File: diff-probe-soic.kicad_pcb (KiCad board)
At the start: 4 copper layers, 75 x 25 mm, 34 parts, among them J1 Conn_01x02, J2 Conn_Coaxial, J3 Conn_01x03, U1 LTC6228xS8, U2 LTC6228xS8, U3 LTC6228xS8

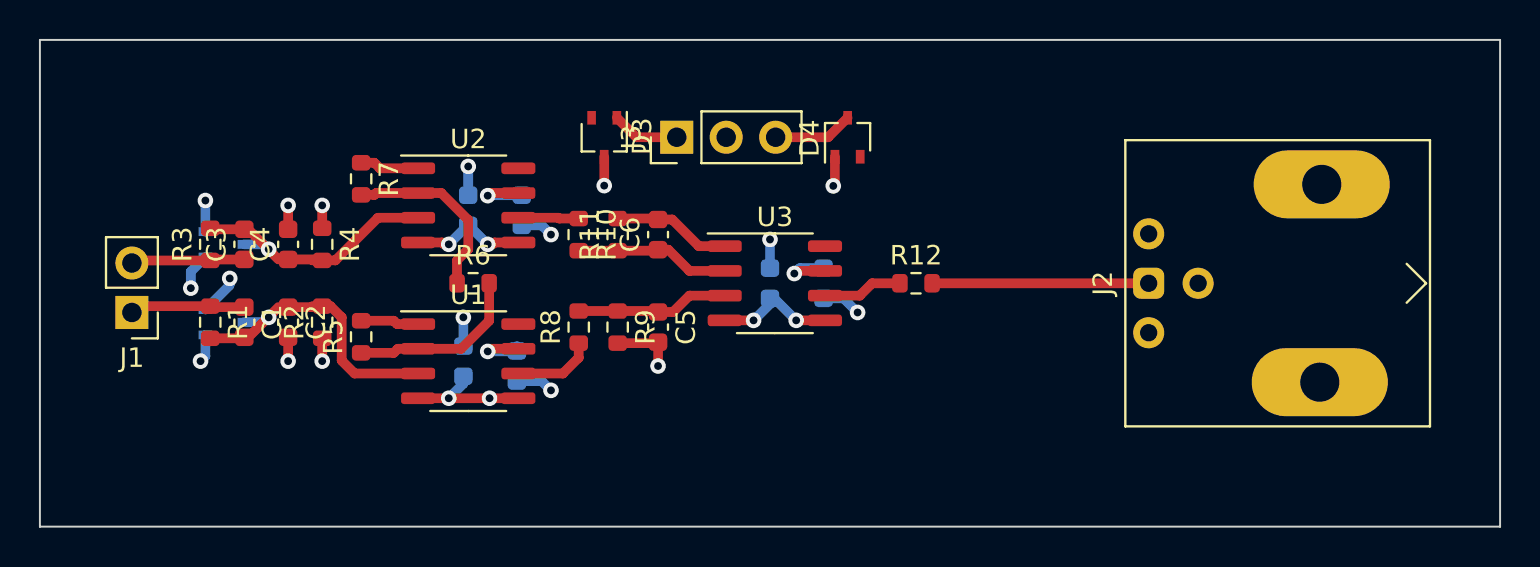
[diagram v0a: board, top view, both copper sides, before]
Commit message: Removed input diodes. Rerouted VDD and VSS.
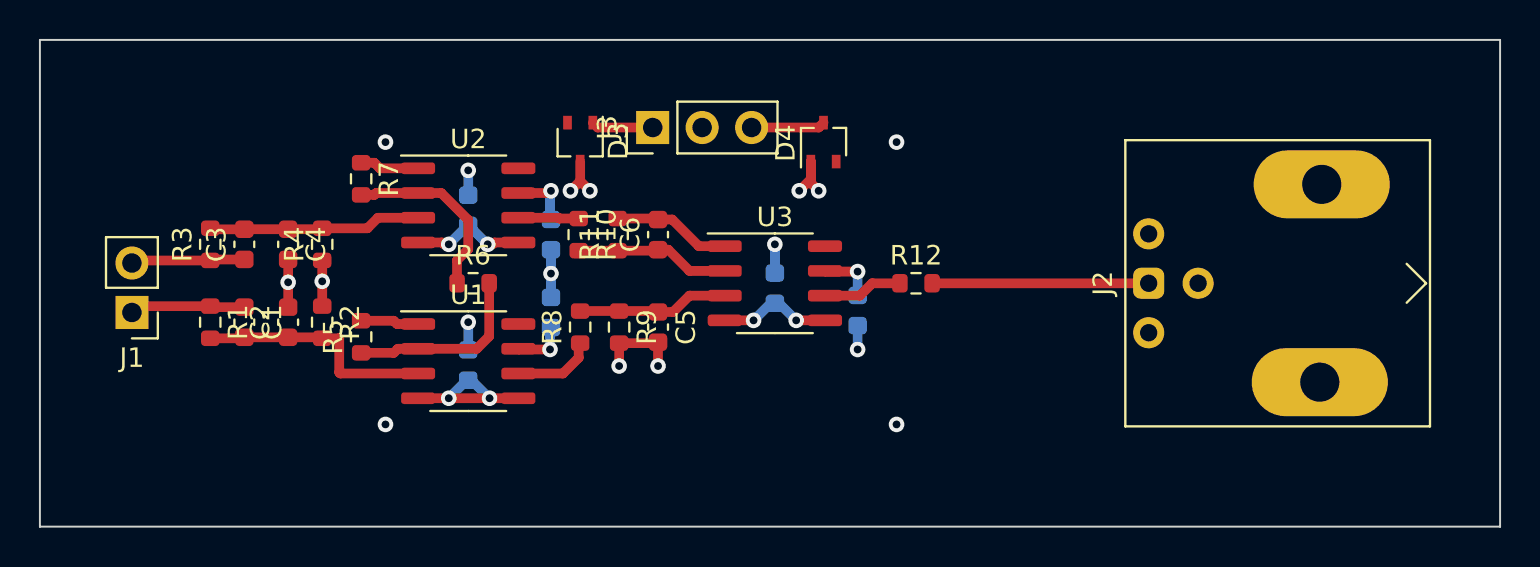
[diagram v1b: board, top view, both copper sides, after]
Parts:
- removed D1, D2: BAT54SW, Package_TO_SOT_SMD:SOT-323_SC-70
- moved C10 3.26 mm to (56.2, 51.5), turned to 90 degrees
- moved C30 2.24 mm to (72.0, 51.4)
- moved C20 1.95 mm to (56.2, 47.5)
- moved J3 1.33 mm to (61.5, 42.0)
- moved D3 1.26 mm to (57.8, 42.8)
- moved D4 1.26 mm to (70.2, 42.8)
- moved C31 0.35 mm to (67.8, 50.2)
- moved C11 0.32 mm to (52.0, 54.2)
- moved R8 0.08 mm to (57.8, 52.2)
- moved R9 0.08 mm to (59.8, 52.2)
- turned C2 to 90 degrees
- turned C4 to -90 degrees
- turned R2 to -90 degrees
- turned R4 to 90 degrees
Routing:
- net VDD: track 66.1 -> 11.2 mm, vias 6 -> 5
- net VSS: track 76.0 -> 23.1 mm, vias 9 -> 8
- net /ATTEN_POS: track 15.3 -> 12.5 mm, vias 1 -> 0
- net /ATTEN_NEG: track 13.5 -> 11.2 mm, vias 1 -> 0
- net GND: track 18.4 -> 16.4 mm, vias 11 -> 13

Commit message: cleaned up power planes. Power connector on south edge. BNC connector is wrong footprint.
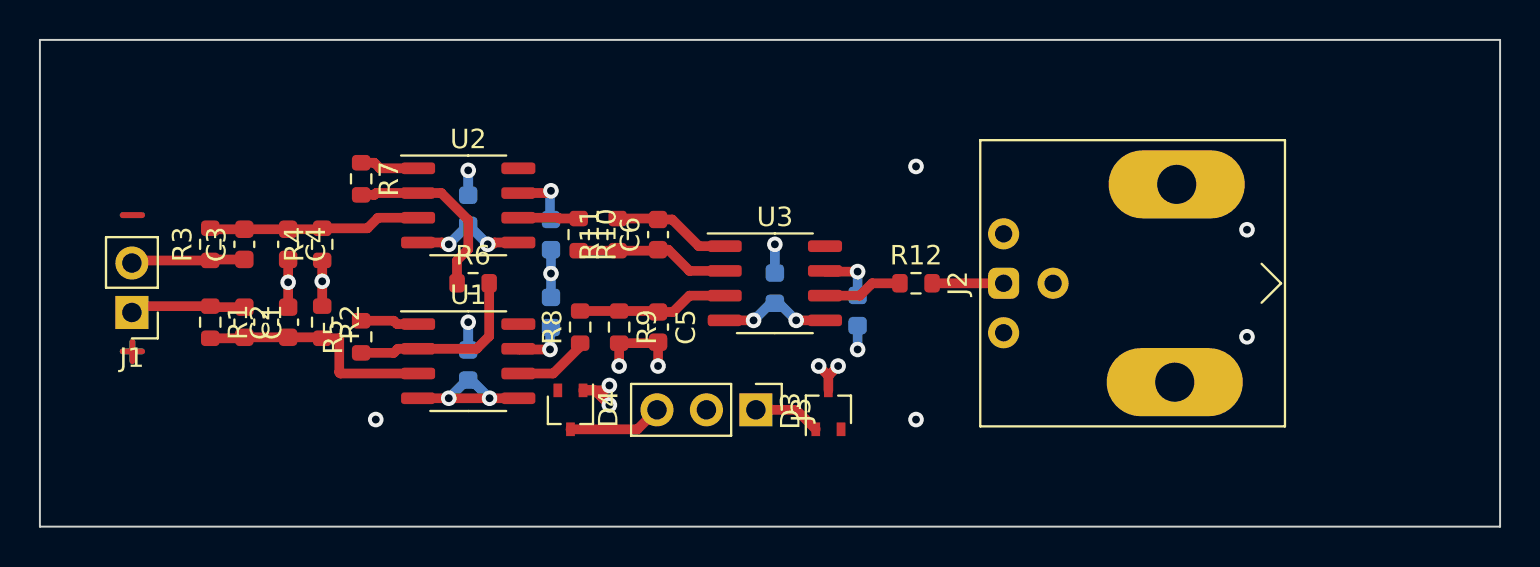
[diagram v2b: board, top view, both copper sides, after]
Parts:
- moved D4 18.9 mm to (57.2, 56.5), turned to -90 degrees
- moved D3 18.8 mm to (70.5, 56.5), turned to 90 degrees
- moved J3 15.4 mm to (66.8, 56.5), turned to -90 degrees
- moved J2 7.45 mm to (79.5, 50.0)
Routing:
- net /OUT: track 11.2 -> 3.67 mm
- net Net-(D4-Pad3): track 3.80 -> 4.86 mm
- net GND: vias 13 -> 14

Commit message: Fixed BNC connector, Moved power connector to east edge on back side.
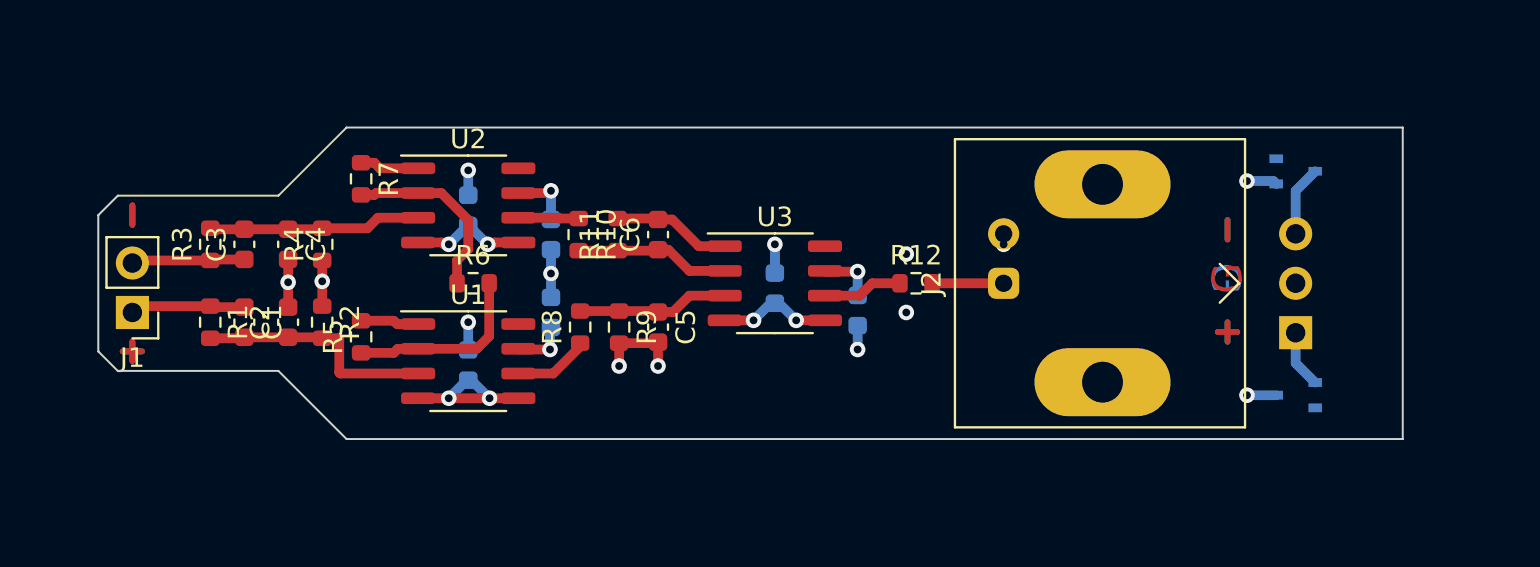
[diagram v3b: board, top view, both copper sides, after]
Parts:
- D3, D4, J3: moved to B.Cu
- J2: value Conn_Coaxial -> 73100-0167 (BNC); footprint Connector_Coaxial:BNC_Amphenol_031-6575_Horizontal -> $MyFootprints:BNC_Molex_73100-0167_Horizontal
- moved D4 39.2 mm to (94.5, 44.2), turned to 0 degrees
- moved J3 28.0 mm to (94.5, 52.5), turned to 0 degrees
- moved D3 24.0 mm to (94.5, 55.8), turned to 180 degrees
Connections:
- net Net-(D3-Pad1) renamed /POS
- net Net-(D4-Pad3) renamed /NEG
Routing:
- net VSS: track 22.7 -> 21.3 mm, vias 8 -> 7
- net /NEG: track 4.86 -> 3.62 mm
- net /POS: track 3.49 -> 2.97 mm
- net VDD: track 11.0 -> 10.6 mm, vias 5 -> 4
- net GND: vias 14 -> 12
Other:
- board size 75 x 25 mm -> 67 x 16 mm
- board text added: "G"

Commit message: Clean layout with SOT-323 schottky diodes and no LEDs
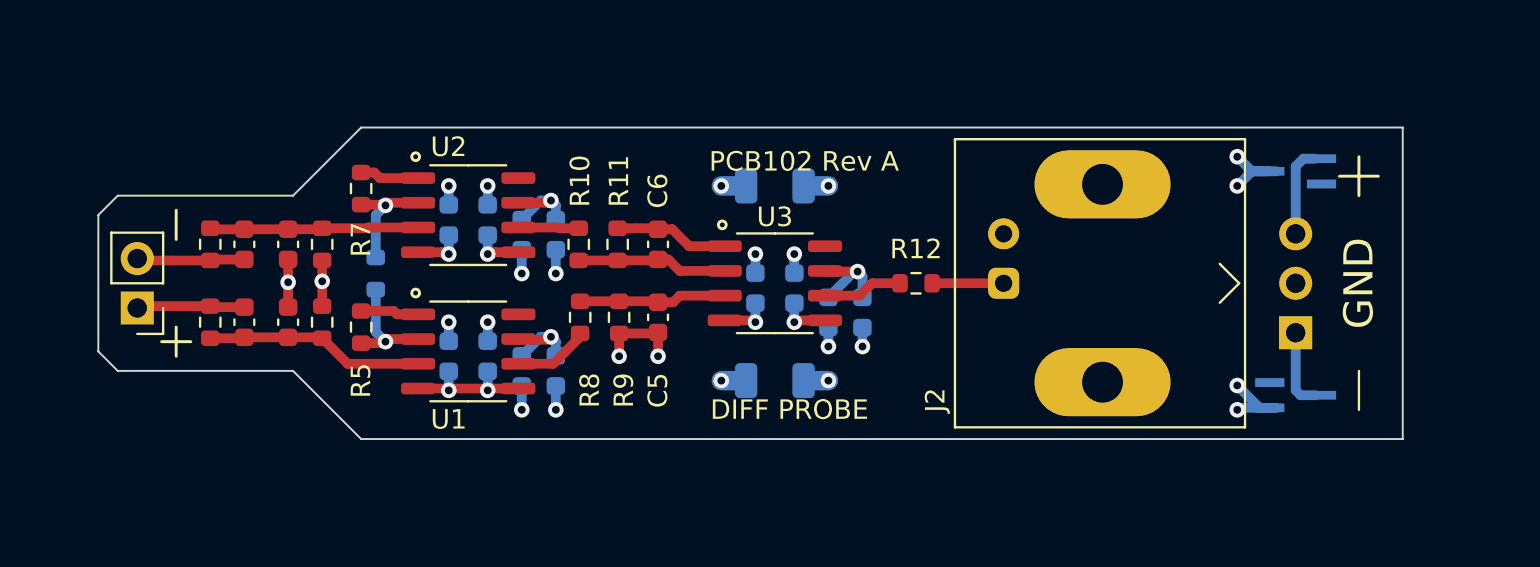
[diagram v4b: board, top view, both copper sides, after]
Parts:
- added C12: 10nF, Capacitor_SMD:C_0603_1608Metric, B.Cu at (54.8, 54.5)
- added C13: 10nF, Capacitor_SMD:C_0603_1608Metric, B.Cu at (51.0, 53.8)
- added C22: 10nF, Capacitor_SMD:C_0603_1608Metric, B.Cu at (54.8, 47.5)
- added C23: 10nF, Capacitor_SMD:C_0603_1608Metric, B.Cu at (51.0, 46.8)
- added C32: 10nF, Capacitor_SMD:C_0603_1608Metric, B.Cu at (70.5, 51.5)
- added C33: 10nF, Capacitor_SMD:C_0603_1608Metric, B.Cu at (66.8, 50.2)
- added C40: 1uF, Capacitor_SMD:C_1206_3216Metric, B.Cu at (67.8, 45.0)
- added C41: 1uF, Capacitor_SMD:C_1206_3216Metric, B.Cu at (67.8, 55.0)
- C1, C3, C5, C6: value 5.6pF -> 3.3pF
- C10, C11, C20, C21, C30, C31: value 1uF -> 1nF
- C2, C4: value 100pF -> 56pF
- D3, D4: footprint Package_TO_SOT_SMD:SOT-323_SC-70 -> Package_TO_SOT_SMD:SOT-323_SC-70_Handsoldering
- J1: footprint Connector_PinHeader_2.54mm:PinHeader_1x02_P2.54mm_Vertical -> Library:PinHeader_1x02_P2.54mm_Vertical
- J2: footprint $MyFootprints:BNC_Molex_73100-0167_Horizontal -> Library:BNC_Molex_73100-0167_Horizontal
- J3: footprint Connector_PinHeader_2.54mm:PinHeader_1x03_P2.54mm_Vertical -> Library:PinHeader_1x03_P2.54mm_Horizontal
- R1, R3: value 215K -> 191K
- R10, R11, R8, R9: value 500 -> 499
- R12: value 50 -> 49.9
- R2, R4: value 11.3K -> 10.0K
- R5, R7: value 500 -> 1K
- R6: value 1K -> 2K; moved to B.Cu
- U1, U2, U3: footprint Package_SO:SO-8_3.9x4.9mm_P1.27mm -> Library:SO-8_3.9x4.9mm_P1.27mm
- moved D3 11.5 mm to (94.5, 44.2)
- moved D4 11.5 mm to (94.5, 55.8)
- moved R6 5.02 mm to (47.2, 49.5), turned to -90 degrees
- moved C10 3.01 mm to (56.5, 54.5), turned to -90 degrees
- moved C21 1.12 mm to (53.0, 46.8)
- moved C11 1.10 mm to (53.0, 53.8)
- moved C31 1.00 mm to (68.8, 50.2)
- moved C5 0.50 mm to (61.8, 51.8)
- moved C6 0.50 mm to (61.8, 48.0)
- moved R10 0.50 mm to (57.7, 48.0)
- moved R11 0.50 mm to (59.7, 48.0)
- moved R5 0.50 mm to (46.5, 52.2)
- moved R7 0.50 mm to (46.5, 45.1)
- moved R8 0.50 mm to (57.8, 51.8)
- moved R9 0.50 mm to (59.8, 51.8)
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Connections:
- J3 pad 1: /POS -> /NEG
- J3 pad 3: /NEG -> /POS
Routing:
- net VDD: track 10.6 -> 20.0 mm, vias 4 -> 6
- net GND: track 16.4 -> 24.1 mm, vias 12 -> 18
- net /FB_POS: track 9.65 -> 5.89 mm, vias 0 -> 1
- net /FB_NEG: track 9.60 -> 5.88 mm, vias 0 -> 1
- net /POS: track 2.97 -> 4.63 mm
- net /ATTEN_POS: track 12.5 -> 11.1 mm
- net VSS: track 21.3 -> 22.6 mm, vias 7 -> 9
- net /ATTEN_NEG: track 11.2 -> 10.6 mm
- net /IN_POS: track 5.93 -> 5.40 mm
- removed copper zone on In2.Cu, net GND
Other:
- outline, holes or cut-outs redrawn
- board text added: "DIFF PROBE"
- board text added: "GND"
- board text added: "PCB102 Rev A"
- board text added: "±5V"
